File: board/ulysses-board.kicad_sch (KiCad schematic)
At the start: 1 part, among them J1 GPIO

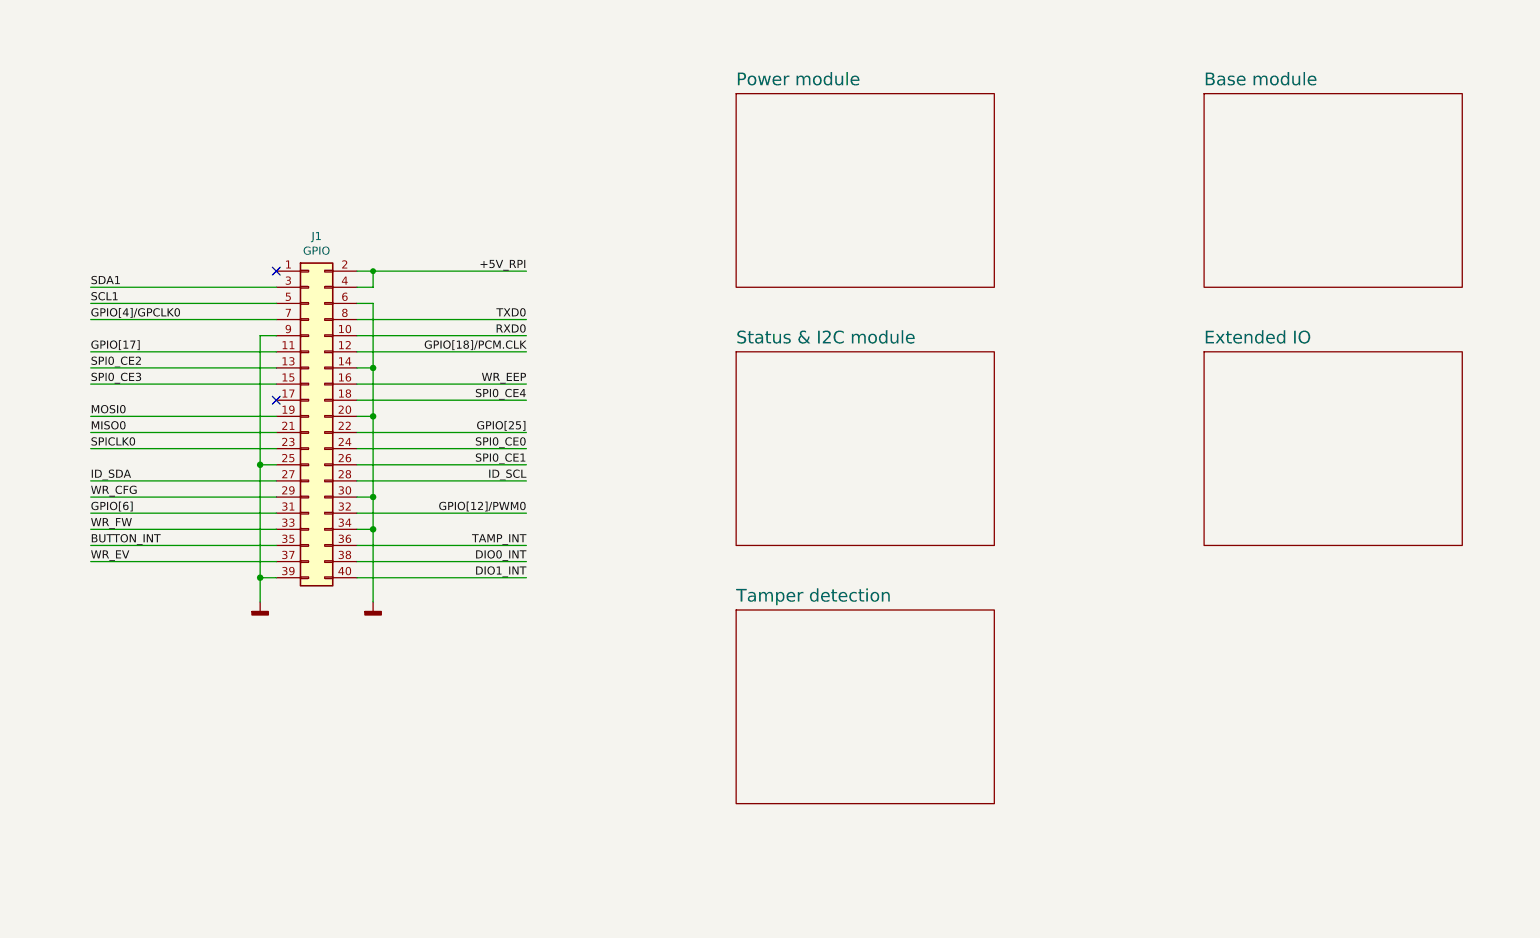
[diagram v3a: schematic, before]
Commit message: Make it a multiboard project.
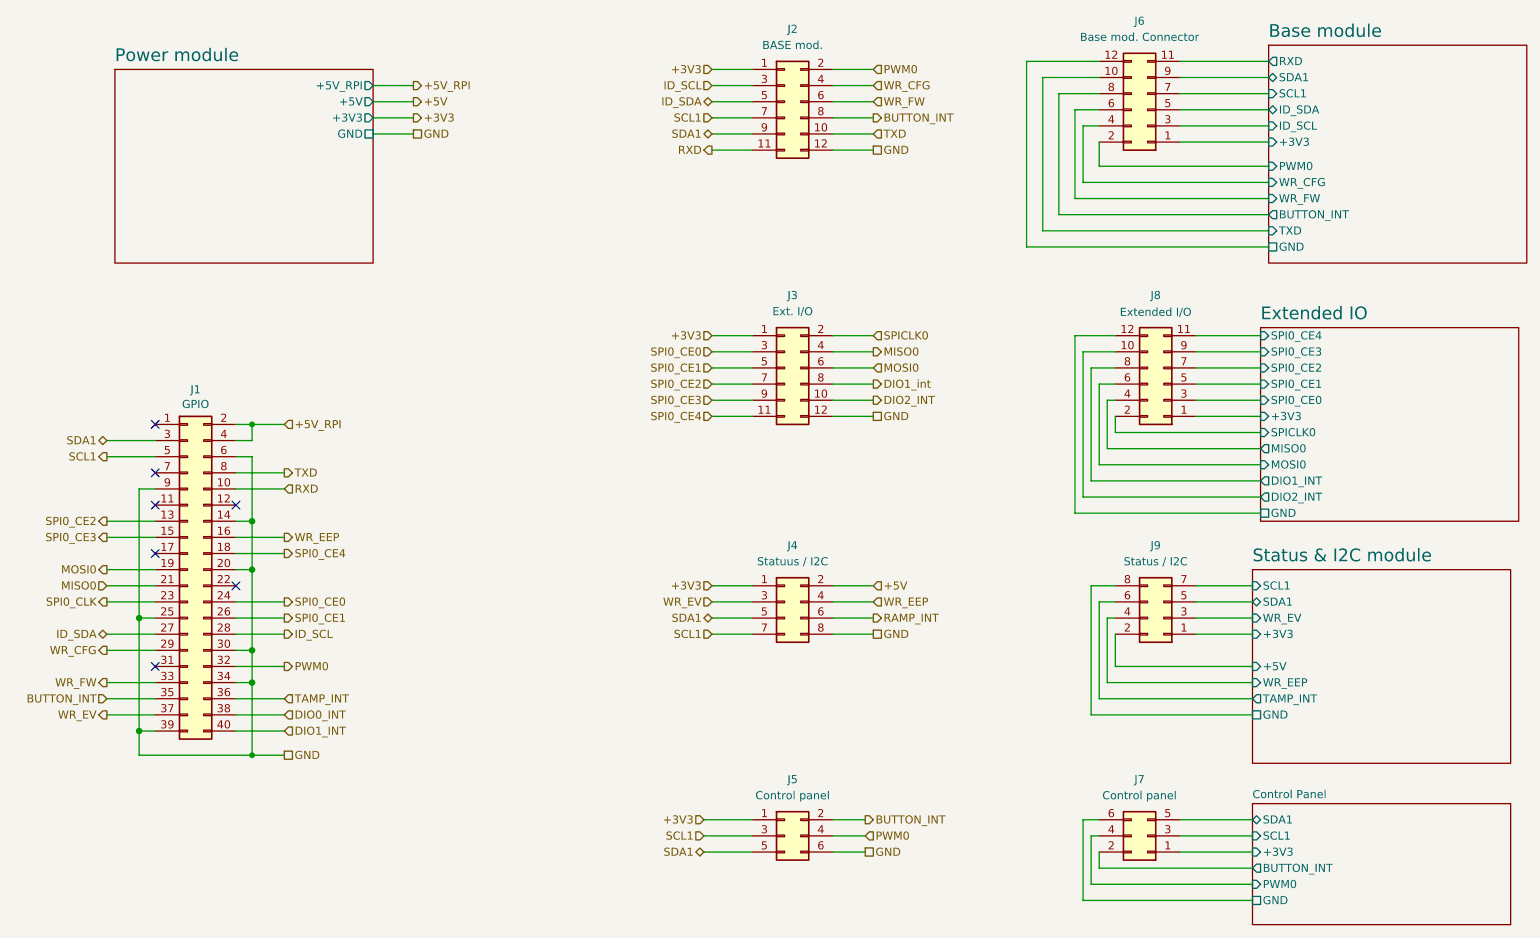
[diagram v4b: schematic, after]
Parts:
- added J2: BASE mod., Connector_PinHeader_2.54mm:PinHeader_2x06_P2.54mm_Vertical, symbol Connector_Generic:Conn_02x06_Odd_Even
- added J3: Ext. I/O, Connector_PinHeader_2.54mm:PinHeader_2x06_P2.54mm_Vertical, symbol Connector_Generic:Conn_02x06_Odd_Even
- added J4: Statuus / I2C, Connector_PinHeader_2.54mm:PinHeader_2x04_P2.54mm_Vertical, symbol Connector_Generic:Conn_02x04_Odd_Even
- added J5, J7: Control panel, Connector_PinHeader_2.54mm:PinHeader_2x03_P2.54mm_Vertical, symbol Connector_Generic:Conn_02x03_Odd_Even
- added J6: Base mod. Connector, Connector_PinHeader_2.54mm:PinHeader_2x06_P2.54mm_Vertical, symbol Connector_Generic:Conn_02x06_Odd_Even
- added J8: Extended I/O, Connector_PinHeader_2.54mm:PinHeader_2x06_P2.54mm_Vertical, symbol Connector_Generic:Conn_02x06_Odd_Even
- added J9: Status / I2C, Connector_PinHeader_2.54mm:PinHeader_2x04_P2.54mm_Vertical, symbol Connector_Generic:Conn_02x04_Odd_Even
- J1: footprint Connector_PinHeader_2.54mm:PinHeader_2x20_P2.54mm_Vertical -> Connector_PinHeader_2.54mm:PinHeader_2x20_P2.54mm_Horizontal
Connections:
- net BUTTON_INT: now also J2.8 (Pin_8), J5.2 (Pin_2)
- net ID_SCL: now also J2.3 (Pin_3)
- net ID_SDA: now also J2.5 (Pin_5)
- net MISO0: now also J3.4 (Pin_4)
- net MOSI0: now also J3.6 (Pin_6)
- net SCL1: now also J2.7 (Pin_7), J4.7 (Pin_7), J5.3 (Pin_3)
- net SDA1: now also J2.9 (Pin_9), J4.5 (Pin_5), J5.5 (Pin_5)
- net SPI0_CE0: now also J3.3 (Pin_3)
- net SPI0_CE1: now also J3.5 (Pin_5)
- net SPI0_CE2: now also J3.7 (Pin_7)
- net SPI0_CE3: now also J3.9 (Pin_9)
- net SPI0_CE4: now also J3.11 (Pin_11)
- net SPICLK0: now also J3.2 (Pin_2); no longer J1.23 (Pin_23)
- net WR_CFG: now also J2.4 (Pin_4)
- net WR_EEP: now also J4.4 (Pin_4)
- net WR_EV: now also J4.3 (Pin_3)
- net WR_FW: now also J2.6 (Pin_6)
- net GNDD renamed GND
- net GND: now also J2.12 (Pin_12), J3.12 (Pin_12), J4.8 (Pin_8), J5.6 (Pin_6)
- net GPIO[12]/PWM0 renamed PWM0
- net PWM0: now also J2.2 (Pin_2), J5.4 (Pin_4)
- net GPIO[17]: no longer names the net of J1.11 (Pin_11)
- net GPIO[18]/PCM.CLK: no longer names the net of J1.12 (Pin_12)
- net GPIO[25]: no longer names the net of J1.22 (Pin_22)
- net GPIO[4]/GPCLK0: no longer names the net of J1.7 (Pin_7)
- net GPIO[6]: no longer names the net of J1.31 (Pin_31)
- net RXD0 renamed RXD
- net RXD: now also J2.11 (Pin_11)
- net TXD0 renamed TXD
- net TXD: now also J2.10 (Pin_10)
- new net +3V3: J2.1 (Pin_1), J3.1 (Pin_1), J4.1 (Pin_1), J5.1 (Pin_1)
- new net +5V: J4.2 (Pin_2)
- new net Base module/+3V3: J6.1 (Pin_1)
- new net Base module/BUTTON_INT: J6.8 (Pin_8)
- new net Base module/GND: J6.12 (Pin_12)
- new net Base module/ID_SCL: J6.3 (Pin_3)
- new net Base module/ID_SDA: J6.5 (Pin_5)
- new net Base module/PWM0: J6.2 (Pin_2)
- new net Base module/RXD: J6.11 (Pin_11)
- new net Base module/SCL1: J6.7 (Pin_7)
- new net Base module/SDA1: J6.9 (Pin_9)
- new net Base module/TXD: J6.10 (Pin_10)
- new net Base module/WR_CFG: J6.4 (Pin_4)
- new net Base module/WR_FW: J6.6 (Pin_6)
- new net Control Panel/+3V3: J7.1 (Pin_1)
- new net Control Panel/BUTTON_INT: J7.2 (Pin_2)
- new net Control Panel/GND: J7.6 (Pin_6)
- new net Control Panel/PWM0: J7.4 (Pin_4)
- new net Control Panel/SCL1: J7.3 (Pin_3)
- new net Control Panel/SDA1: J7.5 (Pin_5)
- new net DIO1_int: J3.8 (Pin_8)
- new net DIO2_INT: J3.10 (Pin_10)
- new net Extended IO/+3V3: J8.1 (Pin_1)
- new net Extended IO/DIO1_INT: J8.8 (Pin_8)
- new net Extended IO/DIO2_INT: J8.10 (Pin_10)
- new net Extended IO/GND: J8.12 (Pin_12)
- new net Extended IO/MISO0: J8.4 (Pin_4)
- new net Extended IO/MOSI0: J8.6 (Pin_6)
- new net Extended IO/SPI0_CE0: J8.3 (Pin_3)
- new net Extended IO/SPI0_CE1: J8.5 (Pin_5)
- new net Extended IO/SPI0_CE2: J8.7 (Pin_7)
- new net Extended IO/SPI0_CE3: J8.9 (Pin_9)
- new net Extended IO/SPI0_CE4: J8.11 (Pin_11)
- new net Extended IO/SPICLK0: J8.2 (Pin_2)
- new net RAMP_INT: J4.6 (Pin_6)
- new net SPI0_CLK: J1.23 (Pin_23)
- new net Status & I2C module/+3V3: J9.1 (Pin_1)
- new net Status & I2C module/+5V: J9.2 (Pin_2)
- new net Status & I2C module/GND: J9.8 (Pin_8)
- new net Status & I2C module/SCL1: J9.7 (Pin_7)
- new net Status & I2C module/SDA1: J9.5 (Pin_5)
- new net Status & I2C module/TAMP_INT: J9.6 (Pin_6)
- new net Status & I2C module/WR_EEP: J9.4 (Pin_4)
- new net Status & I2C module/WR_EV: J9.3 (Pin_3)
- no-connect marks 2 -> 7
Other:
- removed sheet Tamper detection
- added sheet Control Panel (cpanel.kicad_sch)
- sheet Base module ports: added +3V3, BUTTON_INT, GND, ID_SCL, ID_SDA, PWM0, RXD, SCL1, SDA1, TXD, WR_CFG, WR_FW; removed none
- sheet Extended IO ports: added +3V3, DIO1_INT, DIO2_INT, GND, MISO0, MOSI0, SPI0_CE0, SPI0_CE1, SPI0_CE2, SPI0_CE3, SPI0_CE4, SPICLK0; removed none
- sheet Power module ports: added +3V3, +5V, +5V_RPI, GND; removed none
- sheet Status & I2C module ports: added +3V3, +5V, GND, SCL1, SDA1, TAMP_INT, WR_EEP, WR_EV; removed none
- moved on the sheet: J1

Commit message: Modularize board.
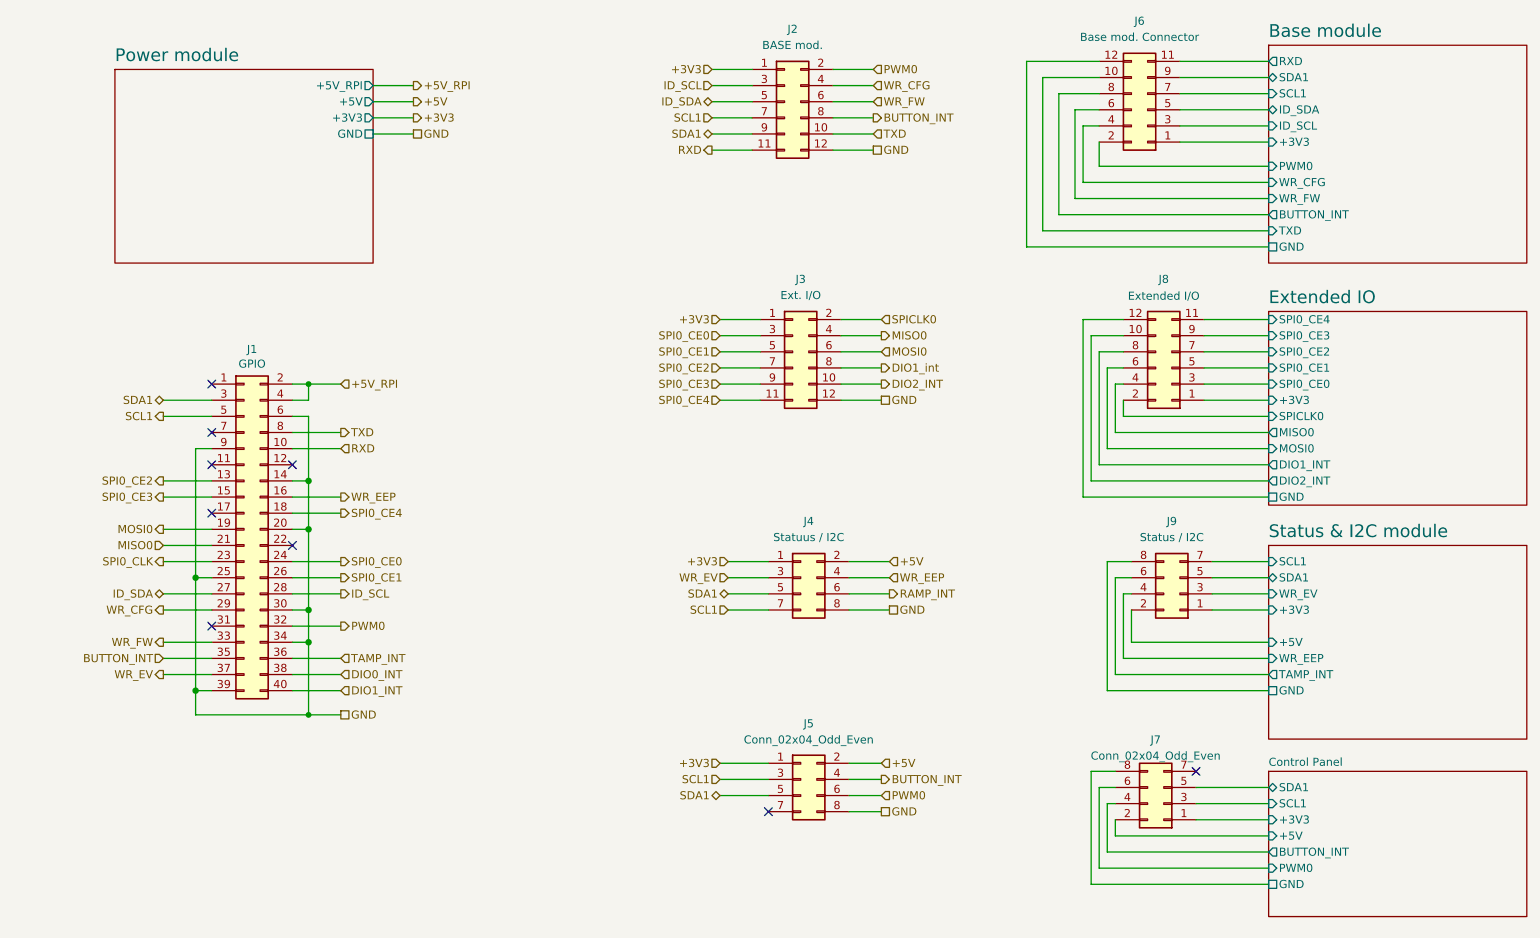
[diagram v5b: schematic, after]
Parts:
- removed J5, J7: Control panel, Connector_PinHeader_2.54mm:PinHeader_2x03_P2.54mm_Vertical, symbol Connector_Generic:Conn_02x03_Odd_Even
- added J5, J7: Conn_02x04_Odd_Even, Connector_PinHeader_2.54mm:PinHeader_2x04_P2.54mm_Vertical, symbol Connector_Generic:Conn_02x04_Odd_Even
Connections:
- net +3V3: now also J5.1 (Pin_1)
- net +5V: now also J5.2 (Pin_2)
- net BUTTON_INT: now also J5.4 (Pin_4)
- net Control Panel/+3V3: now also J7.1 (Pin_1)
- net Control Panel/BUTTON_INT: now also J7.4 (Pin_4)
- net Control Panel/GND: now also J7.8 (Pin_8)
- net Control Panel/PWM0: now also J7.6 (Pin_6)
- net Control Panel/SCL1: now also J7.3 (Pin_3)
- net Control Panel/SDA1: now also J7.5 (Pin_5)
- net GND: now also J5.8 (Pin_8)
- net PWM0: now also J5.6 (Pin_6)
- net SCL1: now also J5.3 (Pin_3)
- net SDA1: now also J5.5 (Pin_5)
- new net Control Panel/+5V: J7.2 (Pin_2)
- no-connect marks 7 -> 9
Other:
- sheet Control Panel ports: added +5V; removed none
- moved on the sheet: J1, J3, J4, J8, J9
